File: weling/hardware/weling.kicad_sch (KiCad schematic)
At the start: 22 parts, among them J1 USB_C_Receptacle_USB2.0_14P, J2 Connector, SW1 BOOT, U1 CH552G, U2 AMS1117-3.3

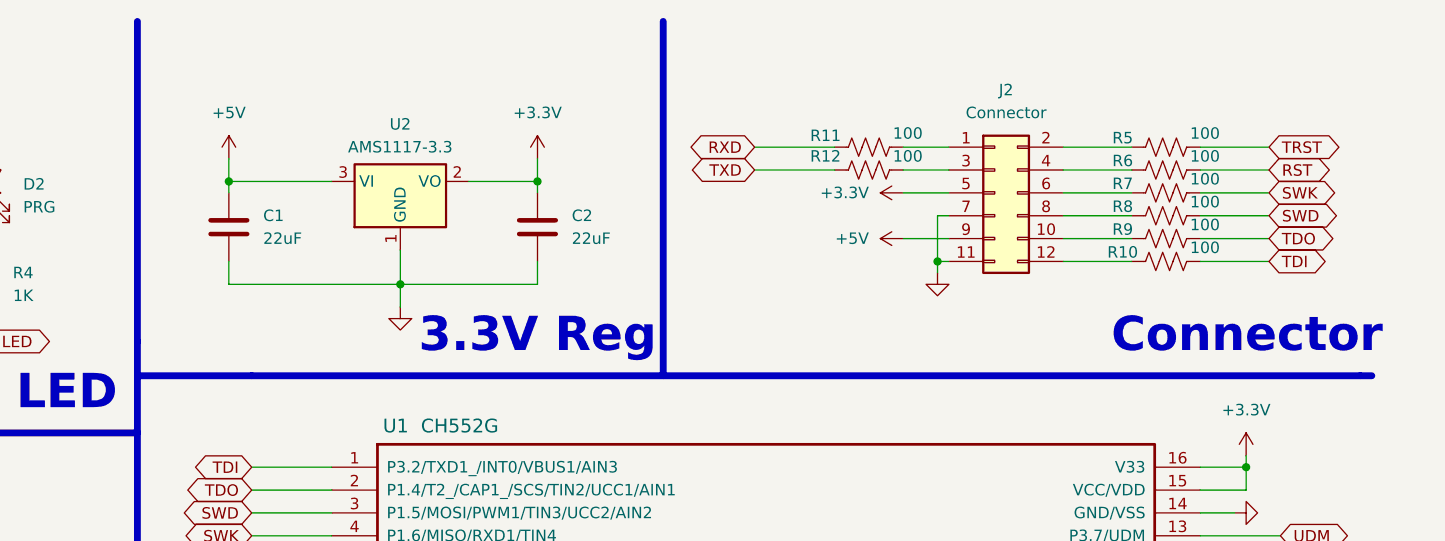
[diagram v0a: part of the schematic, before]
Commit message: feat: add decoupling capacitor
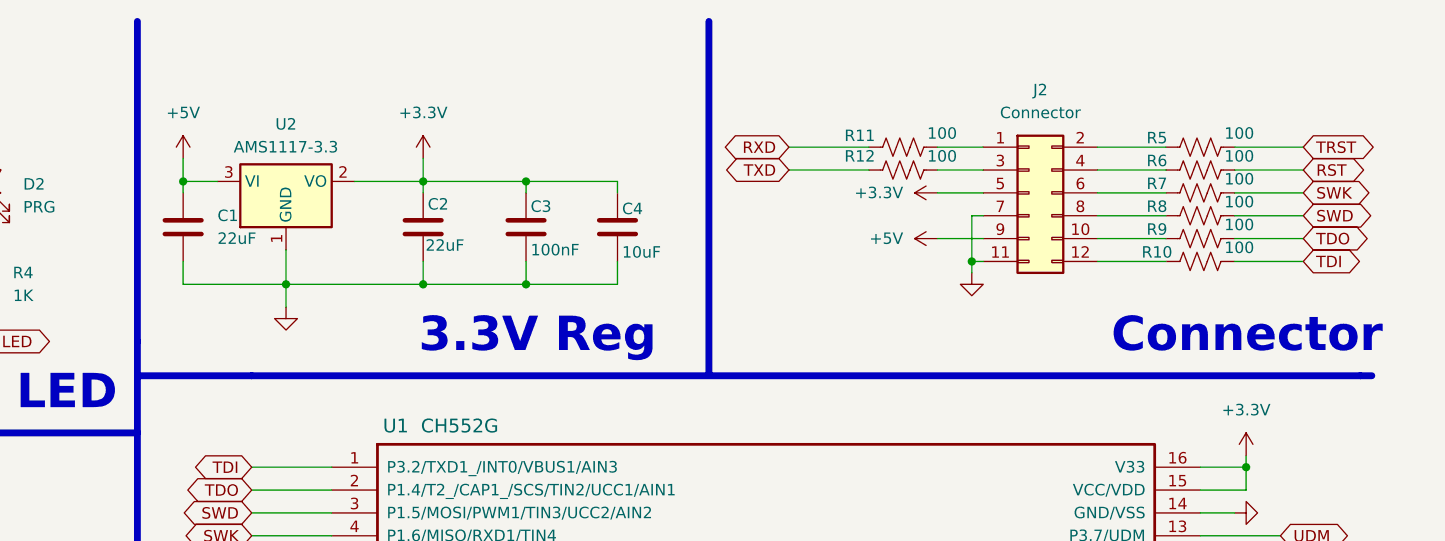
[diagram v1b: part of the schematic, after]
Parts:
- added C3: 100nF, Capacitor_SMD:C_0805_2012Metric_Pad1.18x1.45mm_HandSolder, symbol Device:C
- added C4: 10uF, Capacitor_SMD:C_0805_2012Metric_Pad1.18x1.45mm_HandSolder, symbol Device:C
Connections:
- net +3.3V: now also C3.1, C4.1
- net GND: now also C3.2, C4.2
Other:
- moved on the sheet: C1, C2, J2, R10, R11, R12, R5, R6, R7, R8, R9, U2
